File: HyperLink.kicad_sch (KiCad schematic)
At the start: 41 parts, among them J1 USB_C_Receptacle_USB2.0, J2 Conn_02x05_Odd_Even, J3 Conn_02x05_Odd_Even, SW1 SW_Push, U1 ESP32-C3, U2 LM2937xMP, Y1 ABM11W-40.0000MHZ-8-B1U-T3

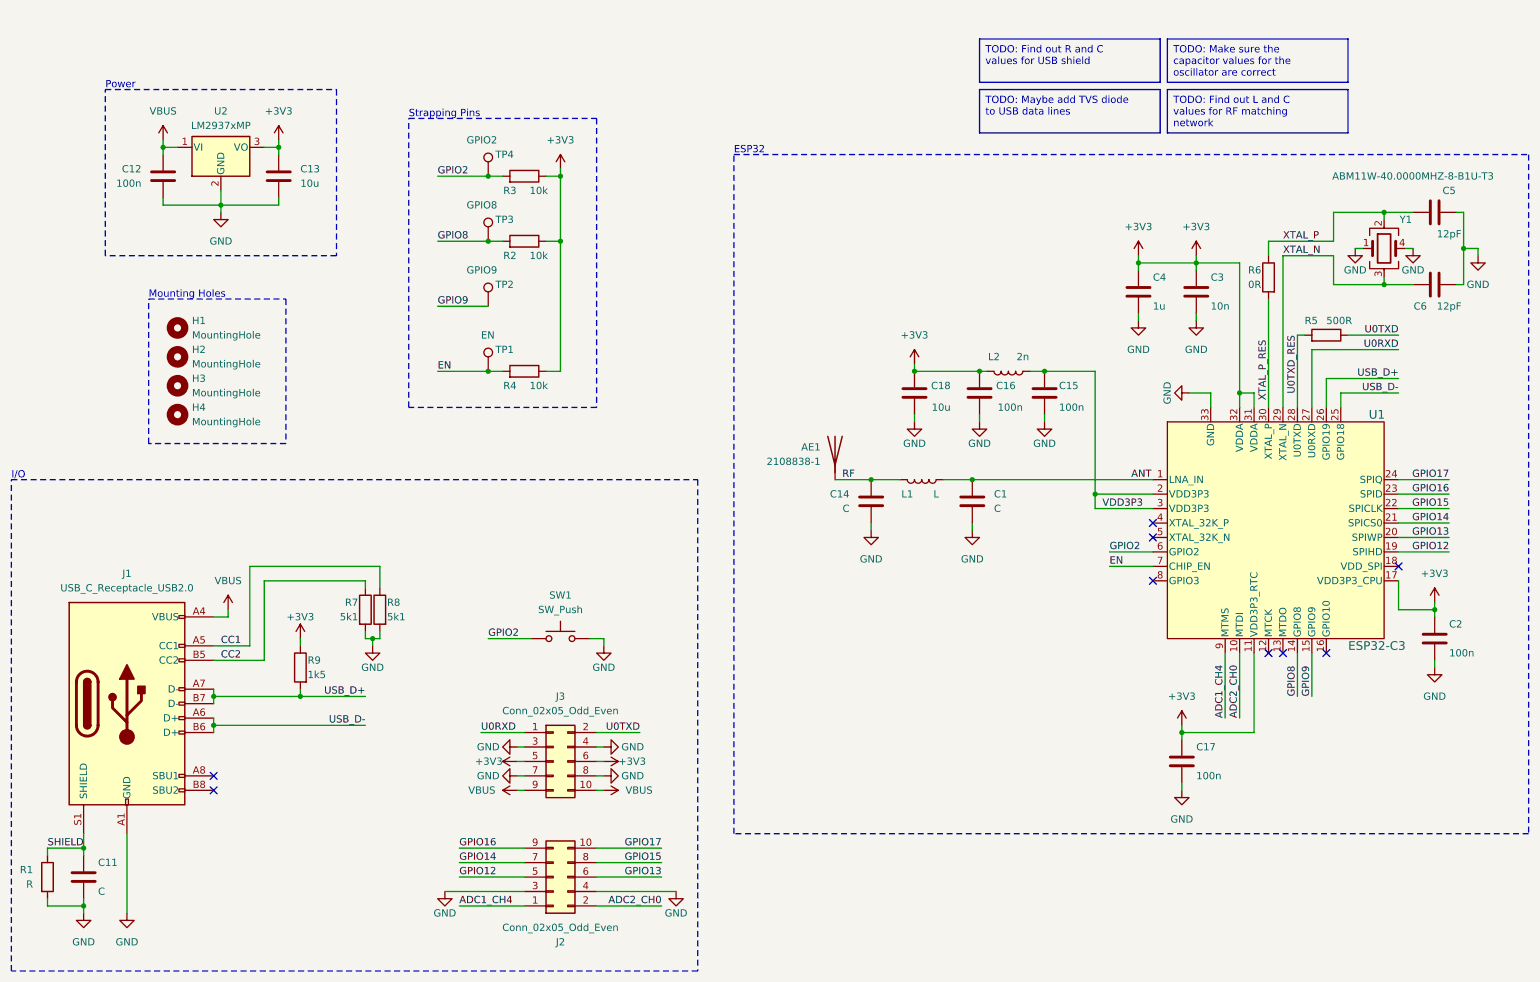
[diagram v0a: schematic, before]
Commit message: Replace LDO and add USB TVS diode
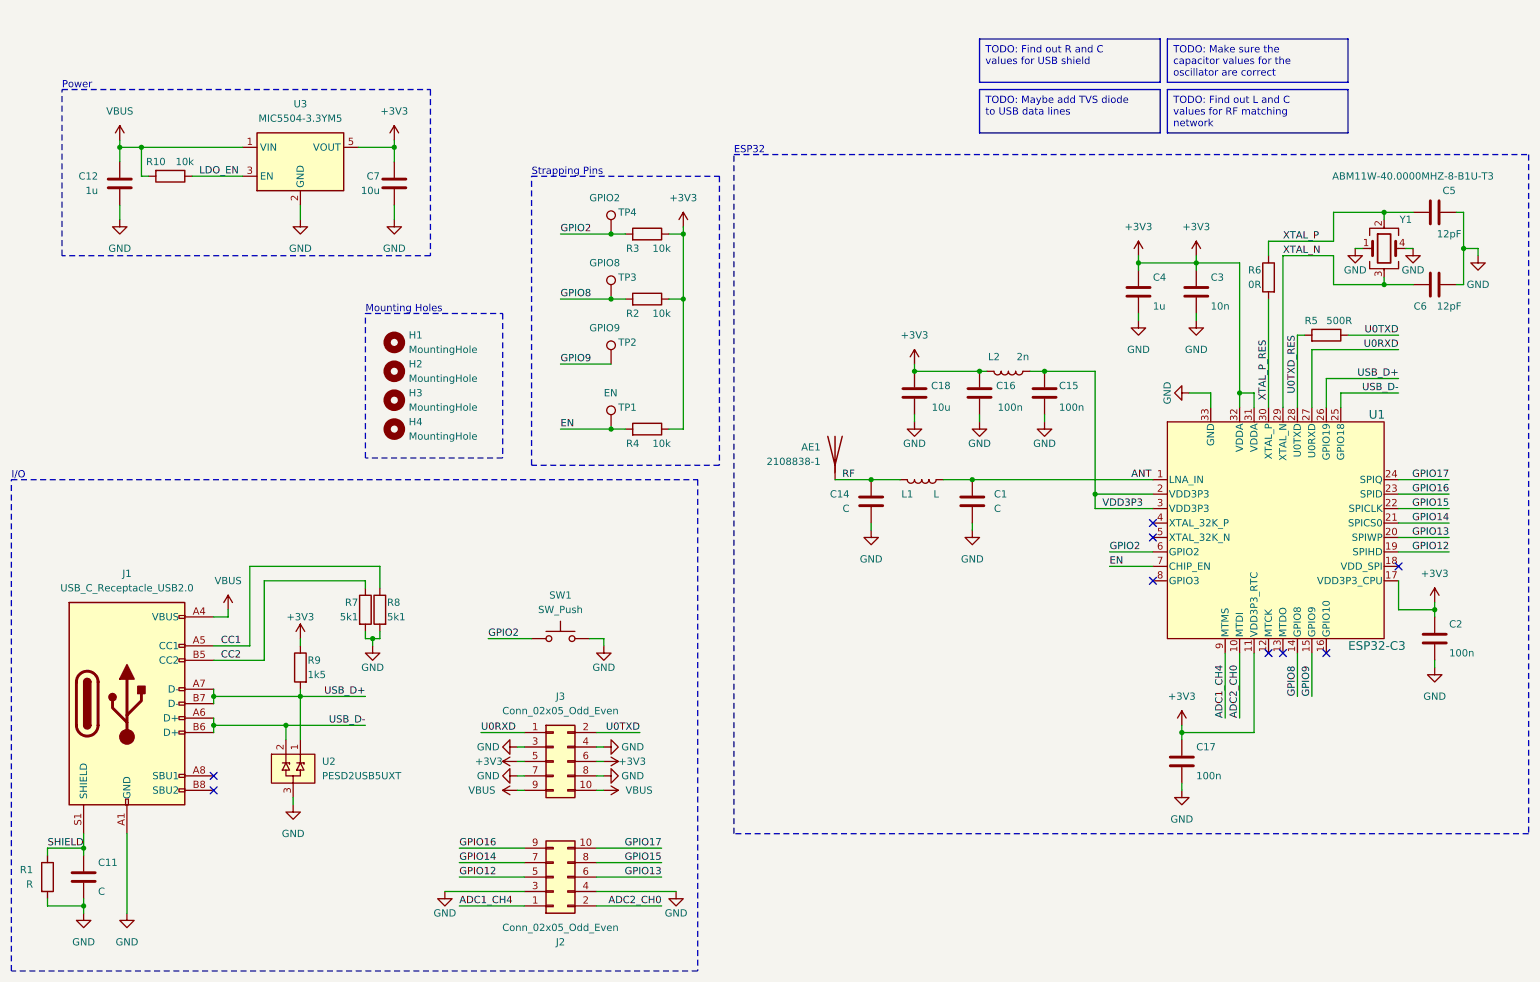
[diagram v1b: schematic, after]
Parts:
- removed C13: 10u, Capacitor_SMD:C_0603_1608Metric, symbol Device:C
- removed U2: LM2937xMP, Package_TO_SOT_SMD:SOT-223-3_TabPin2, symbol Regulator_Linear:LM2937xMP
- added C7: 10u, Capacitor_SMD:C_0603_1608Metric, symbol Device:C
- added R10: 10k, Resistor_SMD:R_0402_1005Metric, symbol Device:R
- added U2: PESD2USB5UXT, Package_TO_SOT_SMD:TSOT-23, symbol encyclopedia_galactica:PESD2USB5UXT
- added U3: MIC5504-3.3YM5, Package_TO_SOT_SMD:SOT-23-5, symbol Regulator_Linear:MIC5504-3.3YM5
- C12: value 100n -> 1u
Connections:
- net +3V3: now also C7.1, U3.5 (VOUT)
- net GND: now also C7.2, U2.3, U3.2 (GND)
- net USB_D+: now also U2.1
- net USB_D-: now also U2.2
- net VBUS: now also R10.2, U3.1 (VIN)
- new net LDO_EN: R10.1, U3.3 (EN)
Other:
- moved on the sheet: C12, H1, H2, H3, H4, R2, R3, R4, TP1, TP2, TP3, TP4

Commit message: Add status LEDs
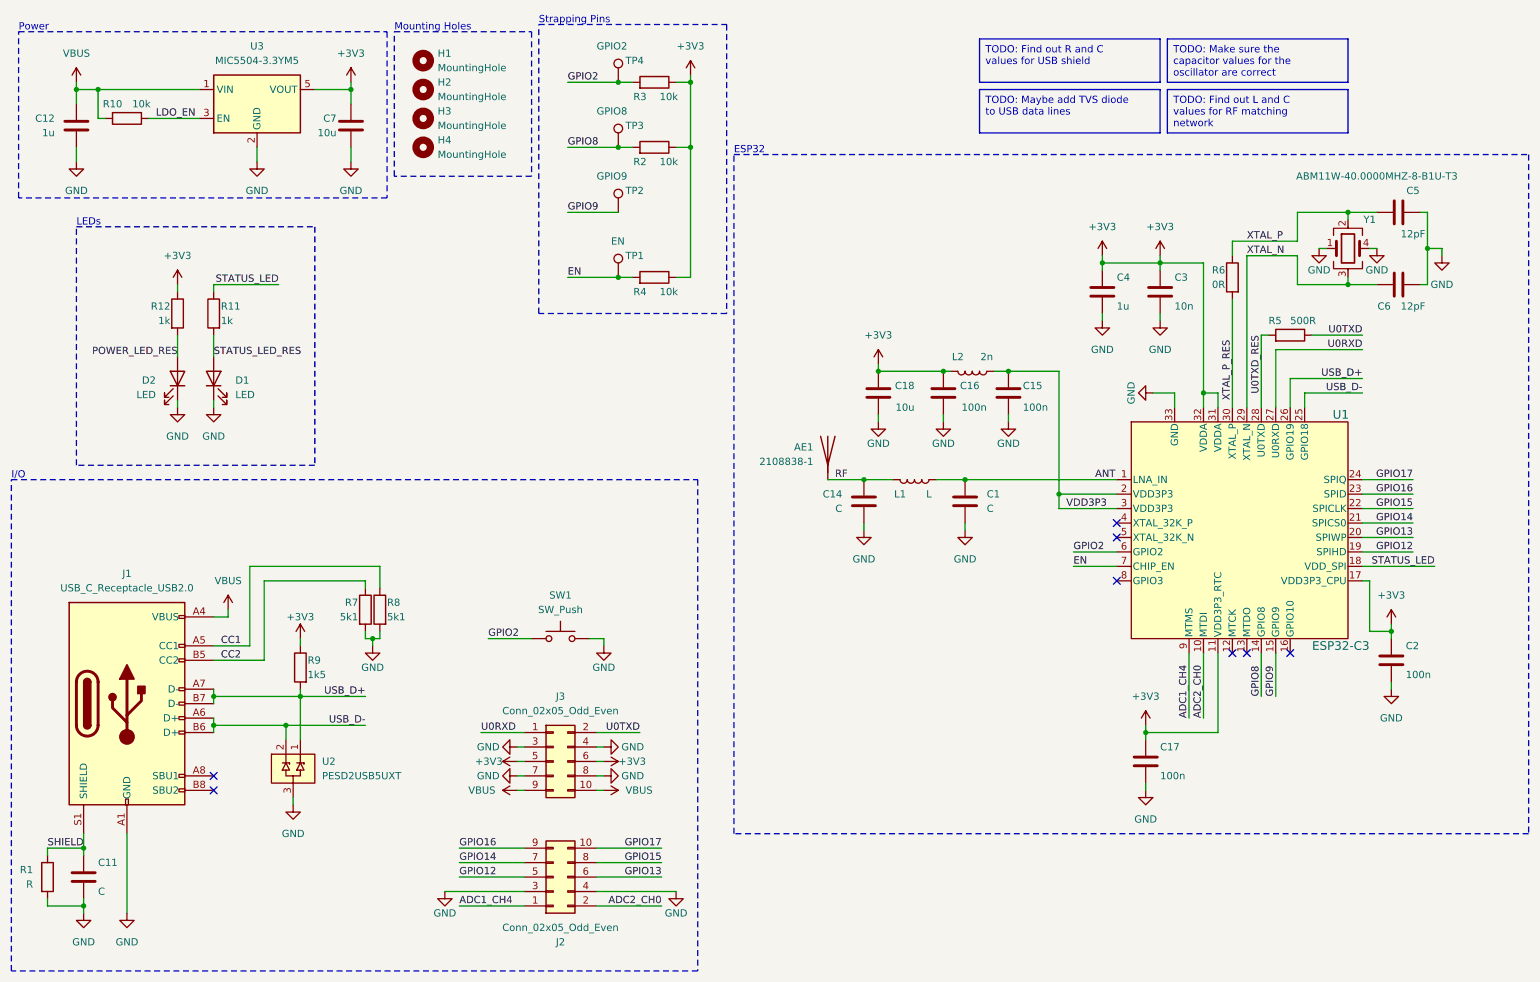
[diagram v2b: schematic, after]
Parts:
- added D1, D2: LED, LED_SMD:LED_0603_1608Metric, symbol Device:LED
- added R11, R12: 1k, Resistor_SMD:R_0402_1005Metric, symbol Device:R
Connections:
- net +3V3: now also R12.1
- net GND: now also D1.1 (K), D2.1 (K)
- net STATUS_LED: now reaches U1.18 (VDD_SPI)
- net STATUS_LED: now also R11.1
- new net POWER_LED_RES: D2.2 (A), R12.2
- new net STATUS_LED_RES: D1.2 (A), R11.2
- no-connect marks 9 -> 8
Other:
- note added: "LEDs"
- moved on the sheet: AE1, C1, C12, C14, C15, C16, C17, C18, C2, C3, C4, C5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
